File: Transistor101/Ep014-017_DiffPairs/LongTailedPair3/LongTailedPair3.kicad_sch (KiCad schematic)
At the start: 17 parts, among them J1 AWG channel 1, J2 AWG channel 2, J3 Output to oscilloscope, Q1 DMMT5551, Q2 DMMT5551, T1 SEE NOTES

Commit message: Transistor 101 - episodes 16-18
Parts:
- removed R2, R3: 300R, symbol Device:R_Small_US
- added C5, C6: 100n, symbol Device:C_Small
- added Q3, Q5: 2N4403, symbol Device:Q_PNP_EBC
- added Q4: 2N4401, symbol Device:Q_NPN_EBC
- added R8: 300R, symbol Device:R_Small_US
- added R9: 12k, symbol Device:R_Small_US
- R5: value 24k -> 3k3
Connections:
- net +12V: now also C5.1, Q4.3 (C), R8.1
- net -12V: now also C6.2, Q5.3 (C), R9.2
- net Earth: now also C5.2, C6.1
- net at Q1.5 (E1): now also Q1.4 (E2), Q2.3 (C2)
- net at Q1.3 (C2), R5.2: now also Q3.2 (B); no longer J3.1 (Pin_1)
- new net: J3.1 (Pin_1), Q4.1 (E), Q5.1 (E)
- new net: Q3.3 (C), Q4.2 (B), Q5.2 (B), R9.1
- new net: Q3.1 (E), R8.2
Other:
- note added: "FOLLOWER STAGE"
- note added: "GAIN STAGE"
- note added: "OSCILLOSCOPE"
- note added: "Place C3, C4 as close to Q1 as possible. Place C5, C6 as close to Q4 and Q5 as possible."
- note added: "This circuit can be breadboarded starting with the circuit from episode 15, modifying R5 from 24k to 3k3, and incrementally adding the gain stage and follower stage. 1. Replace R5, add Q3, R8, R9, C4 and C6; observe common-mode and differential gains at Q3's collector. 2. Add Q4 and Q5. Observe crossover distortion at the output."
- note removed: "Place C3, C4 as close to Q1 as possible."
- note removed: "This circuit can be breadboarded starting with the circuit from episode 14, removing R4 and replacing it with the current source. All other subcircuits are unchanged between the two episodes. Test first with R2 and R3 in place. Then remove R2 and R3 and replace with short circuits. Observe that the gain is improved, the CMRR is unchanged, the circuit remains thermally stable, but large signals su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"
- moved on the sheet: C1, C2, C3, C4, J1, J2, J3, Q1A, Q1B, Q2A, Q2B, R1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

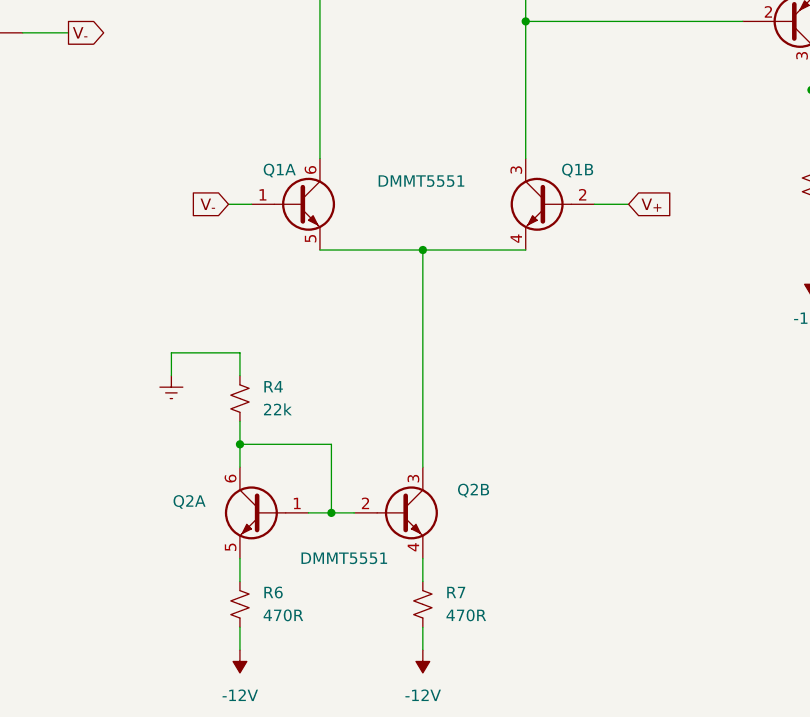
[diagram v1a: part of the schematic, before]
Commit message: Correct pinout of DMMT5401
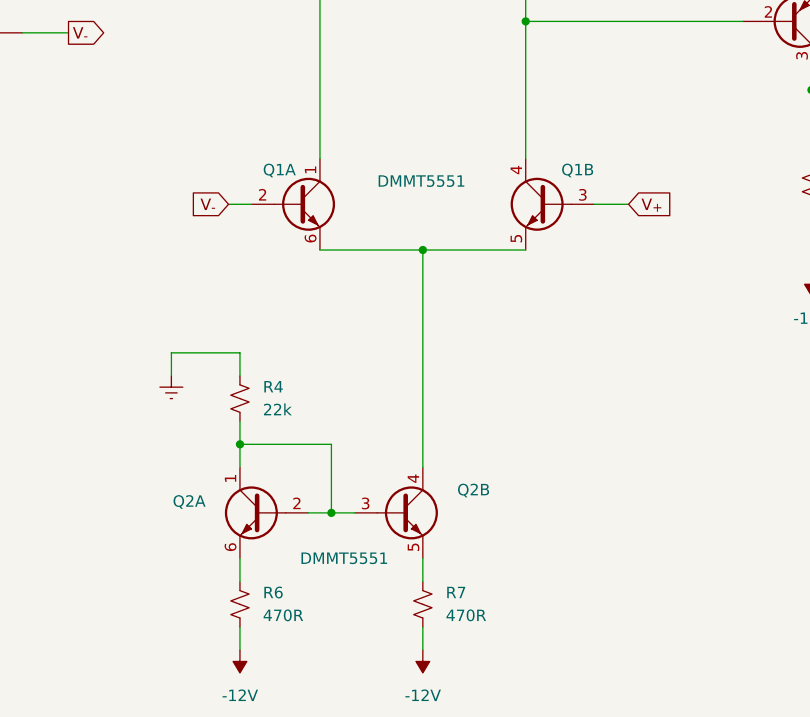
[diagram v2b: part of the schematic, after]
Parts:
- Q1, Q2: footprint (none) -> Package_TO_SOT_SMD:SOT-363_SC-70-6; symbol Kevin-Transistors:Q_Dual_NPN_NPN_B1B2C2E2E1C1 -> Kevin-Transistors:DMMT5551
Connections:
- net +12V: now also Q1.1 (C1); no longer Q1.6 (C1)
- net V_{+}: now also Q1.3 (B2); no longer Q1.2 (B2)
- net V_{-}: now also Q1.2 (B1); no longer Q1.1 (B1)
- net at R6.1: now also Q2.6 (E1); no longer Q2.5 (E1)
- net at Q2.1 (C1), R4.2: now also Q2.2 (B1), Q2.3 (B2); no longer Q2.2 (B2), Q2.6 (C1)
- net at Q3.2 (B), R5.2: now also Q1.4 (C2); no longer Q1.3 (C2)
- net at Q2.4 (C2): now also Q1.5 (E2), Q1.6 (E1); no longer R7.1
- new net: Q2.5 (E2), R7.1
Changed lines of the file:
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@@
   (title_block
     (title "Long-tailed pair: the basic circuit")
-    (date "2025-02-08")
-    (rev "A")
+    (date "2026-05-13")
+    (rev "B")
     (company "Kludges from Kevin's Cave")
     (comment 1 "The differential pair: getting more gain")
@@
     )
   )
-  (symbol (lib_id "Kevin-Transistors:Q_Dual_NPN_NPN_B1B2C2E2E1C1") (at 102.87 109.22 0) (mirror y) (unit 1)
+  (symbol (lib_id "Kevin-Transistors:DMMT5551") (at 102.87 109.22 0) (mirror y) (unit 1)
     (in_bom yes) (on_board yes) (dnp no)
     (property "Reference" "Q2" (at 96.52 107.95 0)
@@
       (effects (font (size 1.27 1.27)) (justify left))
     )
-    (property "Footprint" "" (at 97.79 106.68 0)
-      (effects (font (size 1.27 1.27)) hide)
-    )
-    (property "Datasheet" "~" (at 102.87 109.22 0)
+    (property "Footprint" "Package_TO_SOT_SMD:SOT-363_SC-70-6" (at 97.79 106.68 0)
+      (effects (font (size 1.27 1.27)) hide)
+    )
+    (property "Datasheet" "https://www.diodes.com/assets/Datasheets/ds30436.pdf" (at 102.87 109.22 0)
       (effects (font (size 1.27 1.27)) hide)
     )
@@
     )
   )
-  (symbol (lib_id "Kevin-Transistors:Q_Dual_NPN_NPN_B1B2C2E2E1C1") (at 134.62 74.93 0) (mirror y) (unit 2)
+  (symbol (lib_id "Kevin-Transistors:DMMT5551") (at 134.62 74.93 0) (mirror y) (unit 2)
     (in_bom yes) (on_board yes) (dnp no)
     (property "Reference" "Q1" (at 139.7 71.12 0)
@@
       (effects (font (size 1.27 1.27)) (justify left) hide)
     )
-    (property "Footprint" "" (at 129.54 72.39 0)
-      (effects (font (size 1.27 1.27)) hide)
-    )
-    (property "Datasheet" "~" (at 134.62 74.93 0)
+    (property "Footprint" "Package_TO_SOT_SMD:SOT-363_SC-70-6" (at 129.54 72.39 0)
+      (effects (font (size 1.27 1.27)) hide)
+    )
+    (property "Datasheet" "https://www.diodes.com/assets/Datasheets/ds30436.pdf" (at 134.62 74.93 0)
       (effects (font (size 1.27 1.27)) hide)
     )
@@
     )
   )
-  (symbol (lib_id "Kevin-Transistors:Q_Dual_NPN_NPN_B1B2C2E2E1C1") (at 118.11 109.22 0) (unit 2)
+  (symbol (lib_id "Kevin-Transistors:DMMT5551") (at 118.11 109.22 0) (unit 2)
     (in_bom yes) (on_board yes) (dnp no)
     (property "Reference" "Q2" (at 124.46 106.68 0)
@@
       (effects (font (size 1.27 1.27)) (justify left) hide)
     )
-    (property "Footprint" "" (at 123.19 106.68 0)
-      (effects (font (size 1.27 1.27)) hide)
-    )
-    (property "Datasheet" "~" (at 118.11 109.22 0)
+    (property "Footprint" "Package_TO_SOT_SMD:SOT-363_SC-70-6" (at 123.19 106.68 0)
+      (effects (font (size 1.27 1.27)) hide)
+    )
+    (property "Datasheet" "https://www.diodes.com/assets/Datasheets/ds30436.pdf" (at 118.11 109.22 0)
       (effects (font (size 1.27 1.27)) hide)
     )
@@
     )
   )
-  (symbol (lib_id "Kevin-Transistors:Q_Dual_NPN_NPN_B1B2C2E2E1C1") (at 106.68 74.93 0) (unit 1)
+  (symbol (lib_id "Kevin-Transistors:DMMT5551") (at 106.68 74.93 0) (unit 1)
     (in_bom yes) (on_board yes) (dnp no)
     (property "Reference" "Q1" (at 102.87 71.12 0)
@@
       (effects (font (size 1.27 1.27)) (justify left))
     )
-    (property "Footprint" "" (at 111.76 72.39 0)
-      (effects (font (size 1.27 1.27)) hide)
-    )
-    (property "Datasheet" "~" (at 106.68 74.93 0)
-      (effects (font (size 1.27 1.27)) hide)
-    )
+    (property "Footprint" "Package_TO_SOT_SMD:SOT-363_SC-70-6" (at 111.76 72.39 0)
+      (effects (font (size 1.27 1.27)) hide)
+    )
+    (property "Datasheet" "https://www.diodes.com/assets/Datasheets/ds30436.pdf" (at 106.68 74.93 0)
+      (effects (font (size 1.27 1.27)) hide)
+    )
